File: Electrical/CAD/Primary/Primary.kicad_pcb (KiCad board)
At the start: 2 copper layers, 82 x 144 mm, 18 parts, among them Q1 2N3904, Q2 2N3906, SW1 SW_DPST, U1 LMC555xN, U2 MCP6282

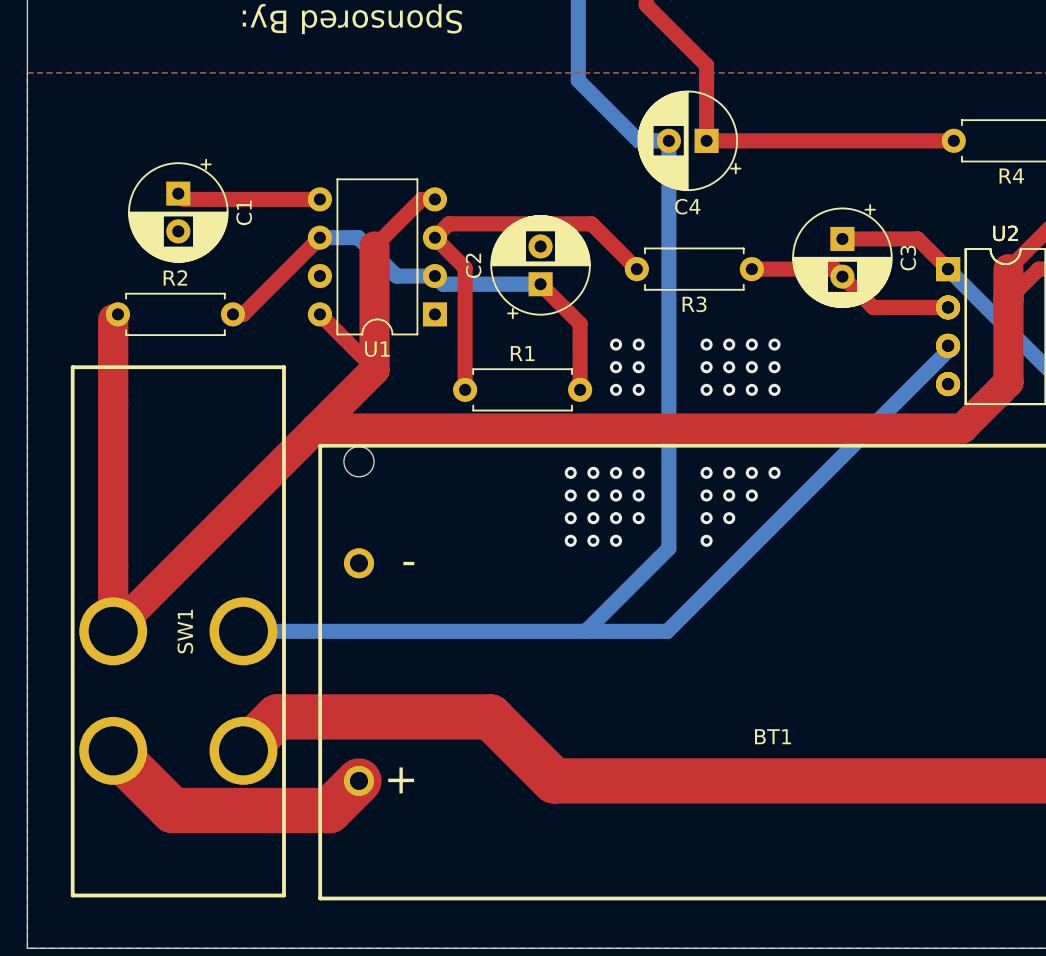
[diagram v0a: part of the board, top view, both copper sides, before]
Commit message: Modified footprints for caps and battery on primary PCB.
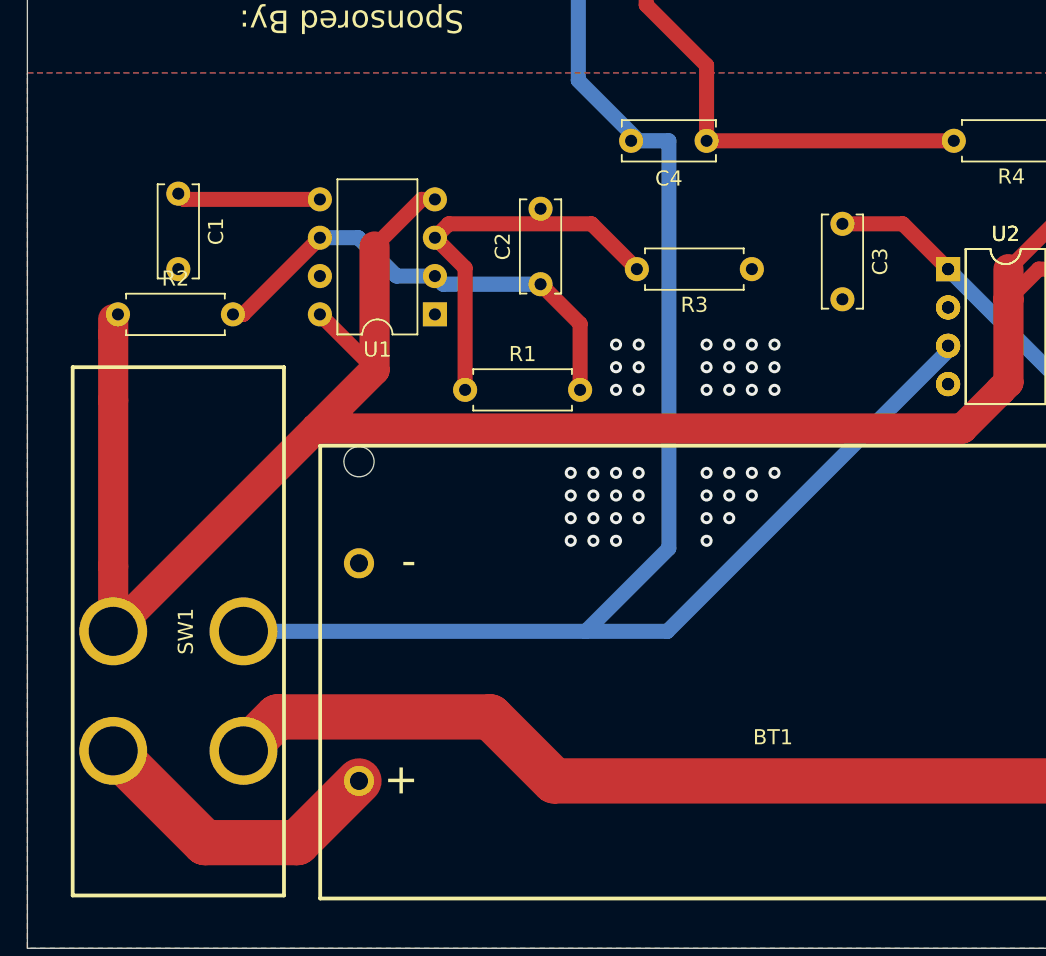
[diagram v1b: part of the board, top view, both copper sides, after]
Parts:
- C1, C2, C3, C4: footprint Capacitor_THT:CP_Radial_D6.3mm_P2.50mm -> Capacitor_THT:C_Disc_D6.0mm_W2.5mm_P5.00mm
- moved C3 1.00 mm to (186.6, 111.3)
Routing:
- net Net-(C3-Pad2): track 14.1 -> 0.00 mm
- net Net-(BT1-Pad1): track 18.7 -> 20.5 mm

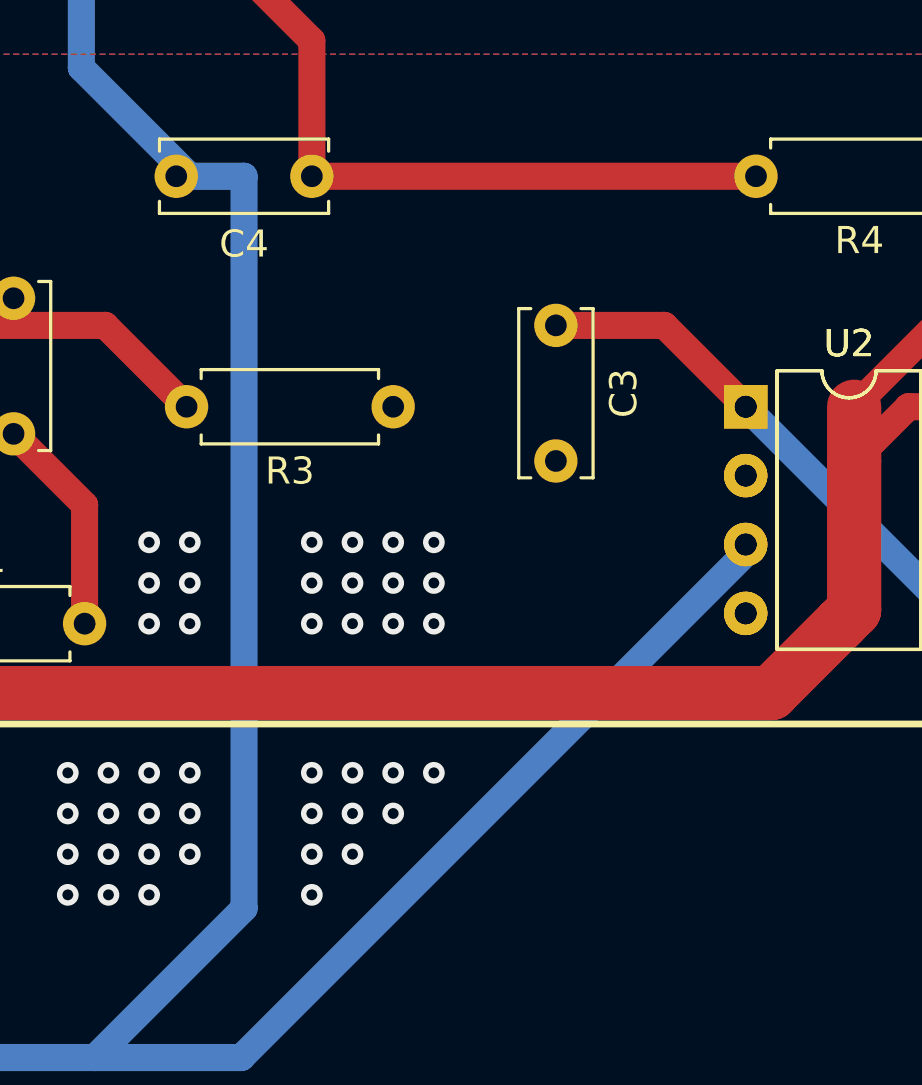
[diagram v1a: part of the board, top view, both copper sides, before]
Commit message: PCB: fix route to new capacitor footprints
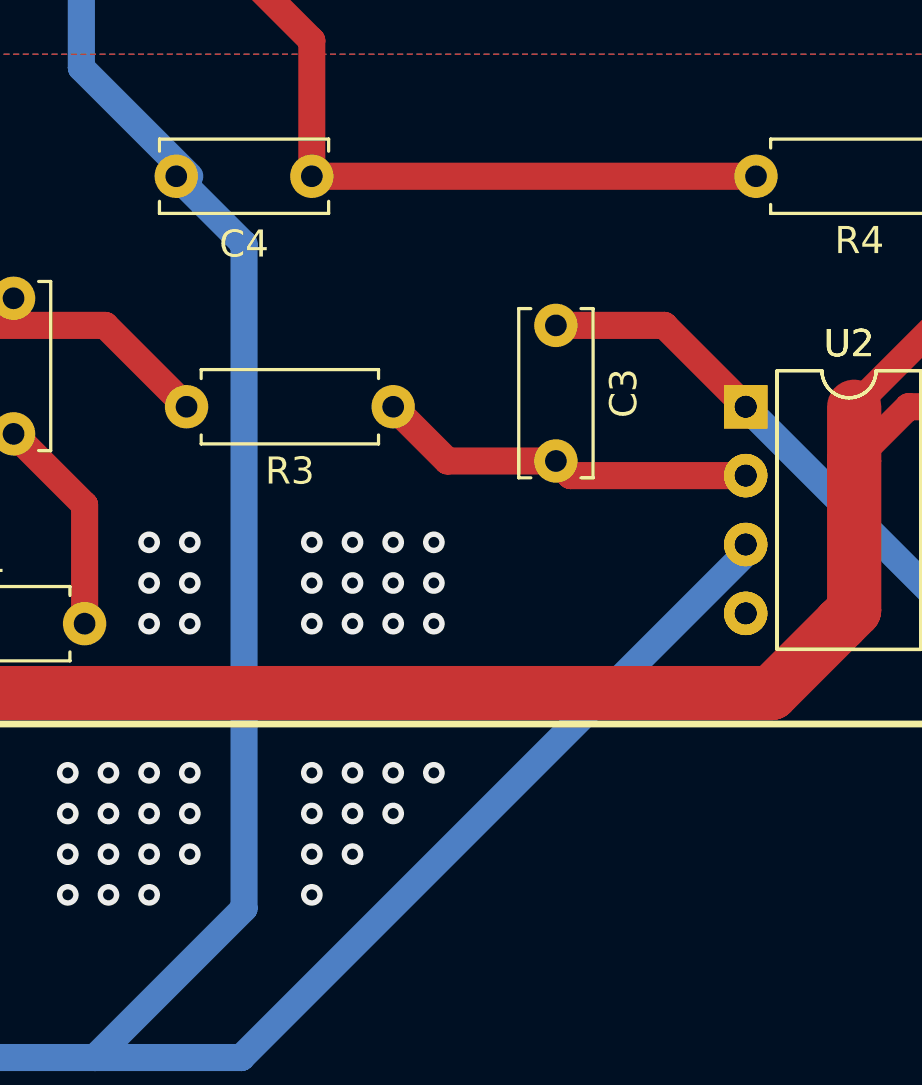
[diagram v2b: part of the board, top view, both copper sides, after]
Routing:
- net Net-(C3-Pad2): track 0.00 -> 14.1 mm
- net +1V5: track 139.9 -> 138.9 mm

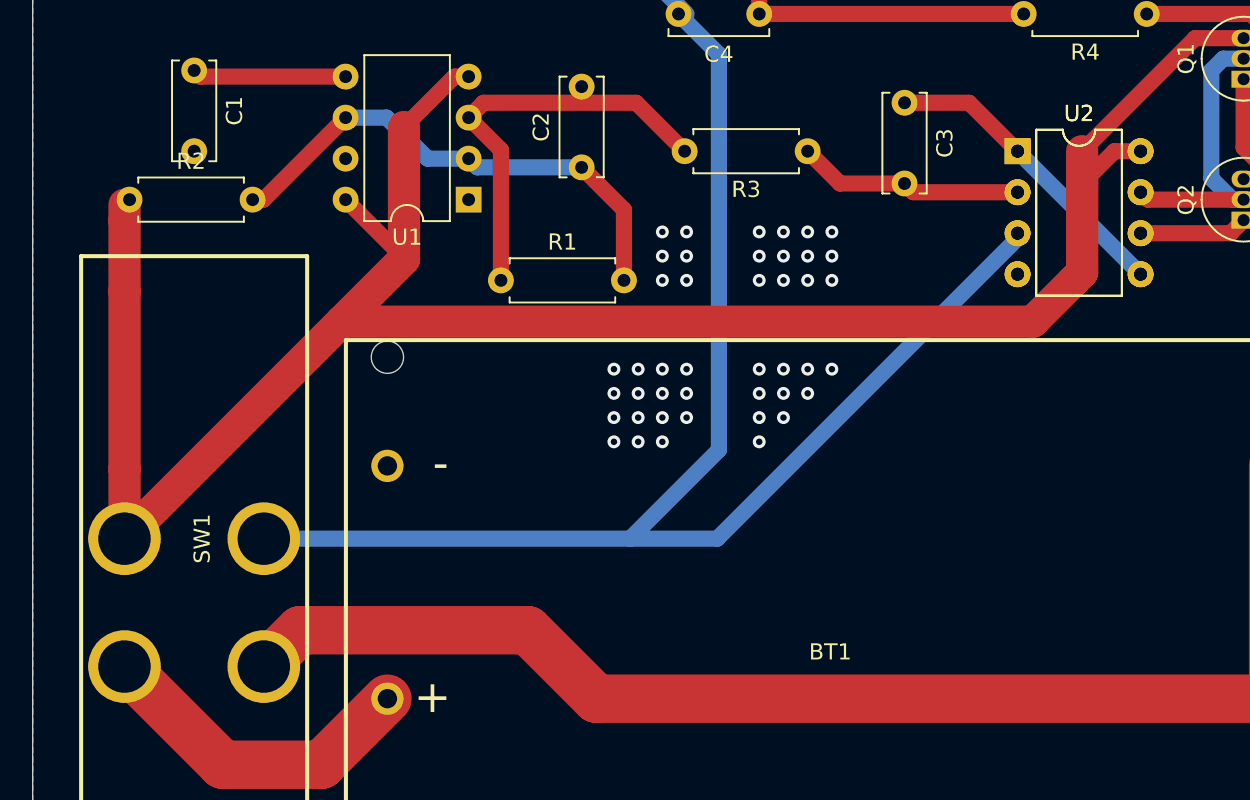
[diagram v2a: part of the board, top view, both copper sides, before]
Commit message: PCB: change pads for switch to slots
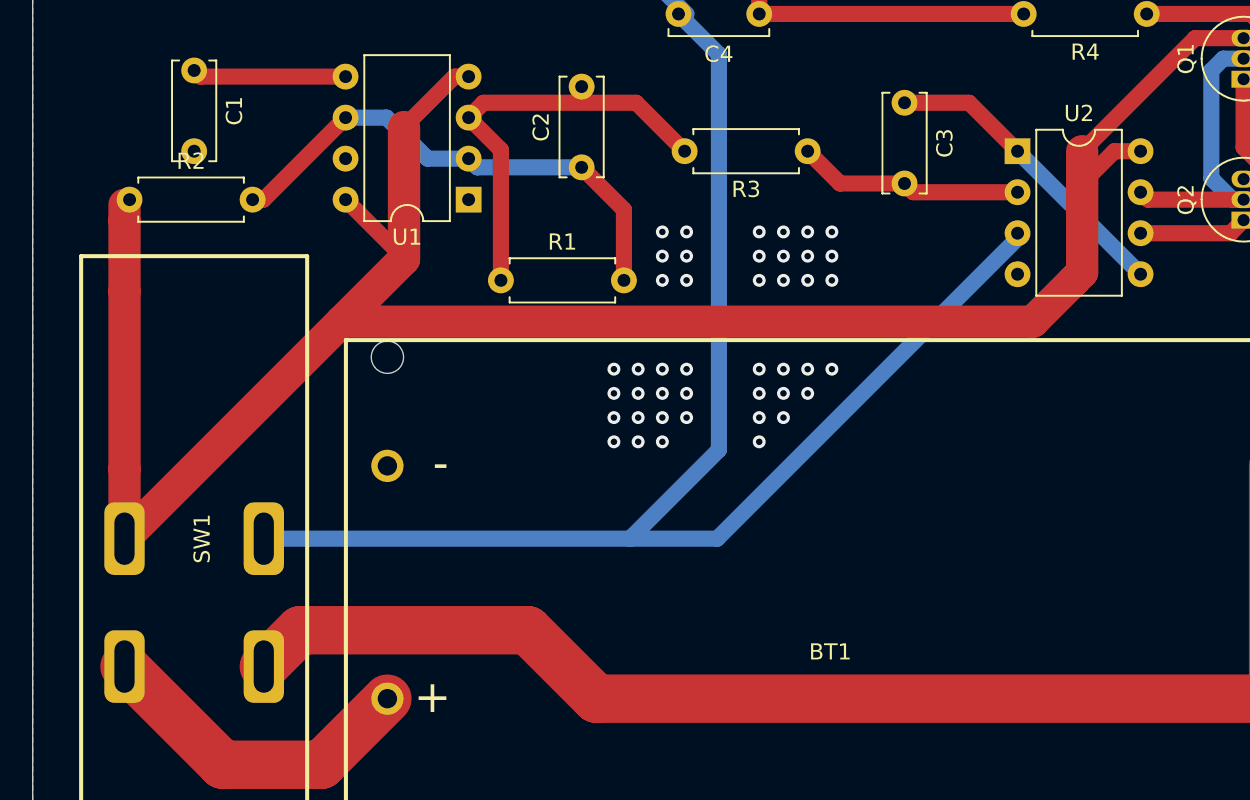
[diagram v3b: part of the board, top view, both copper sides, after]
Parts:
- removed the U2 at (193.6, 114.3)

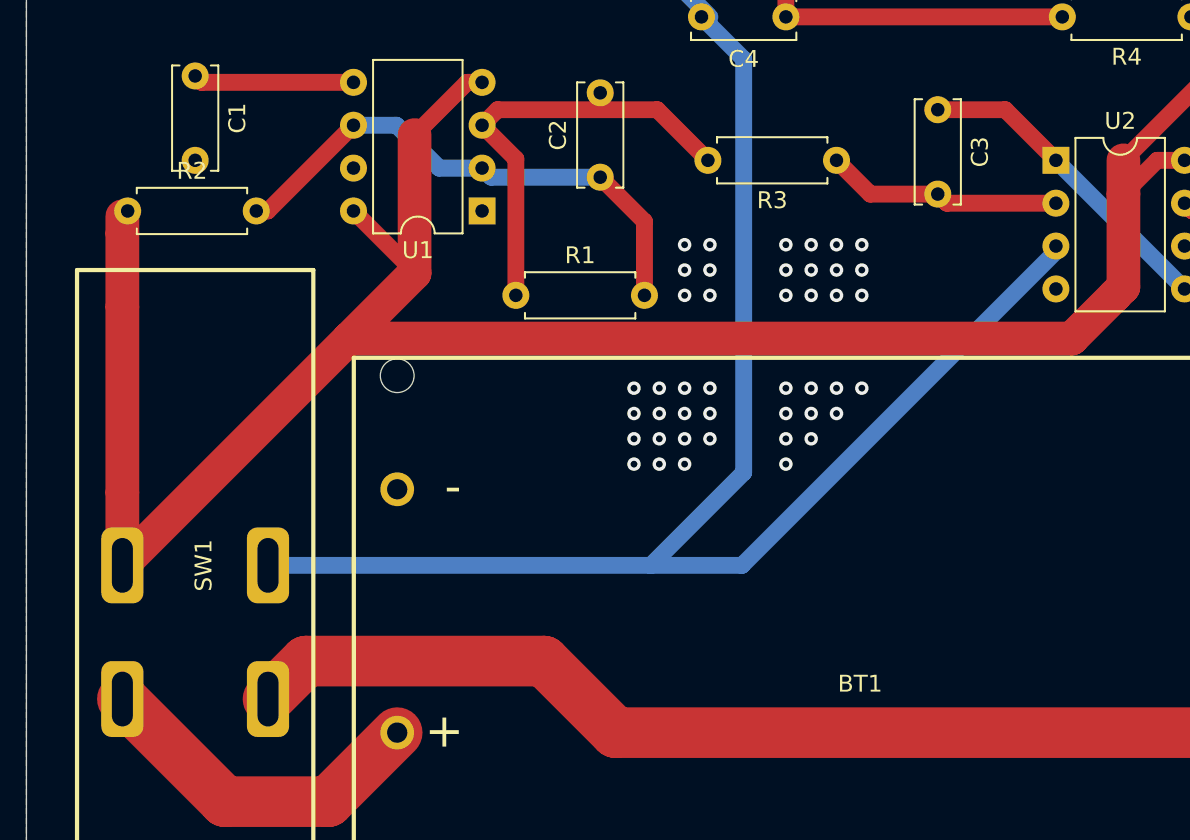
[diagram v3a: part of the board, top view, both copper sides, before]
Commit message: PCB: fix remaining tracks that were too close to pins, make slots for switch .25mm longer
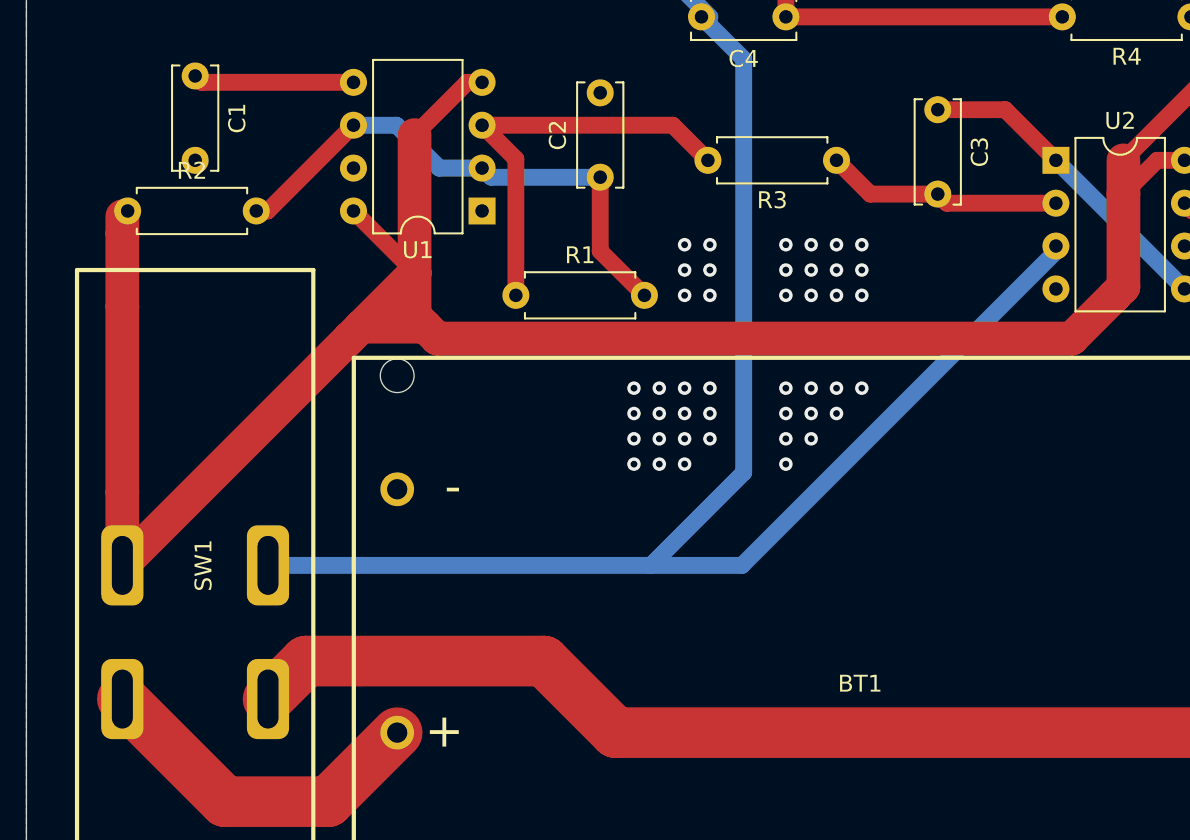
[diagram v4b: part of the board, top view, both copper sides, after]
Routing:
- net +3V0: track 136.3 -> 139.3 mm
- net Net-(R1-Pad1): track 25.9 -> 25.1 mm
